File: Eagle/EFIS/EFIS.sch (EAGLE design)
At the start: 17 parts

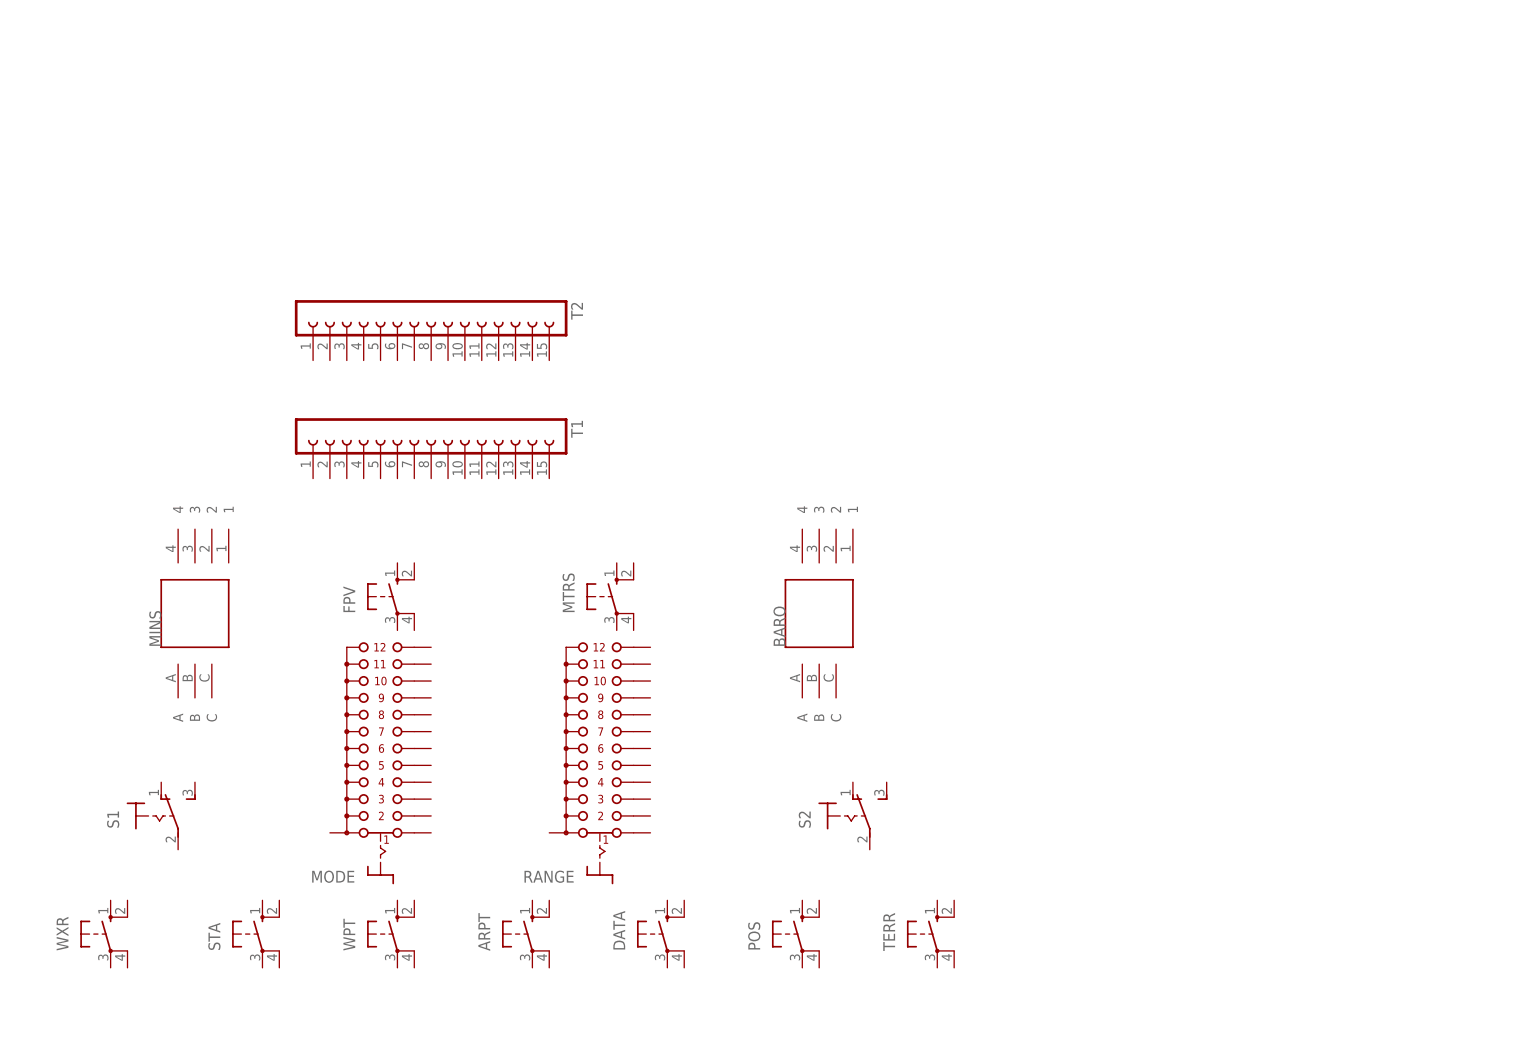
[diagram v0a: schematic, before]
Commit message: Button connections in Eagle
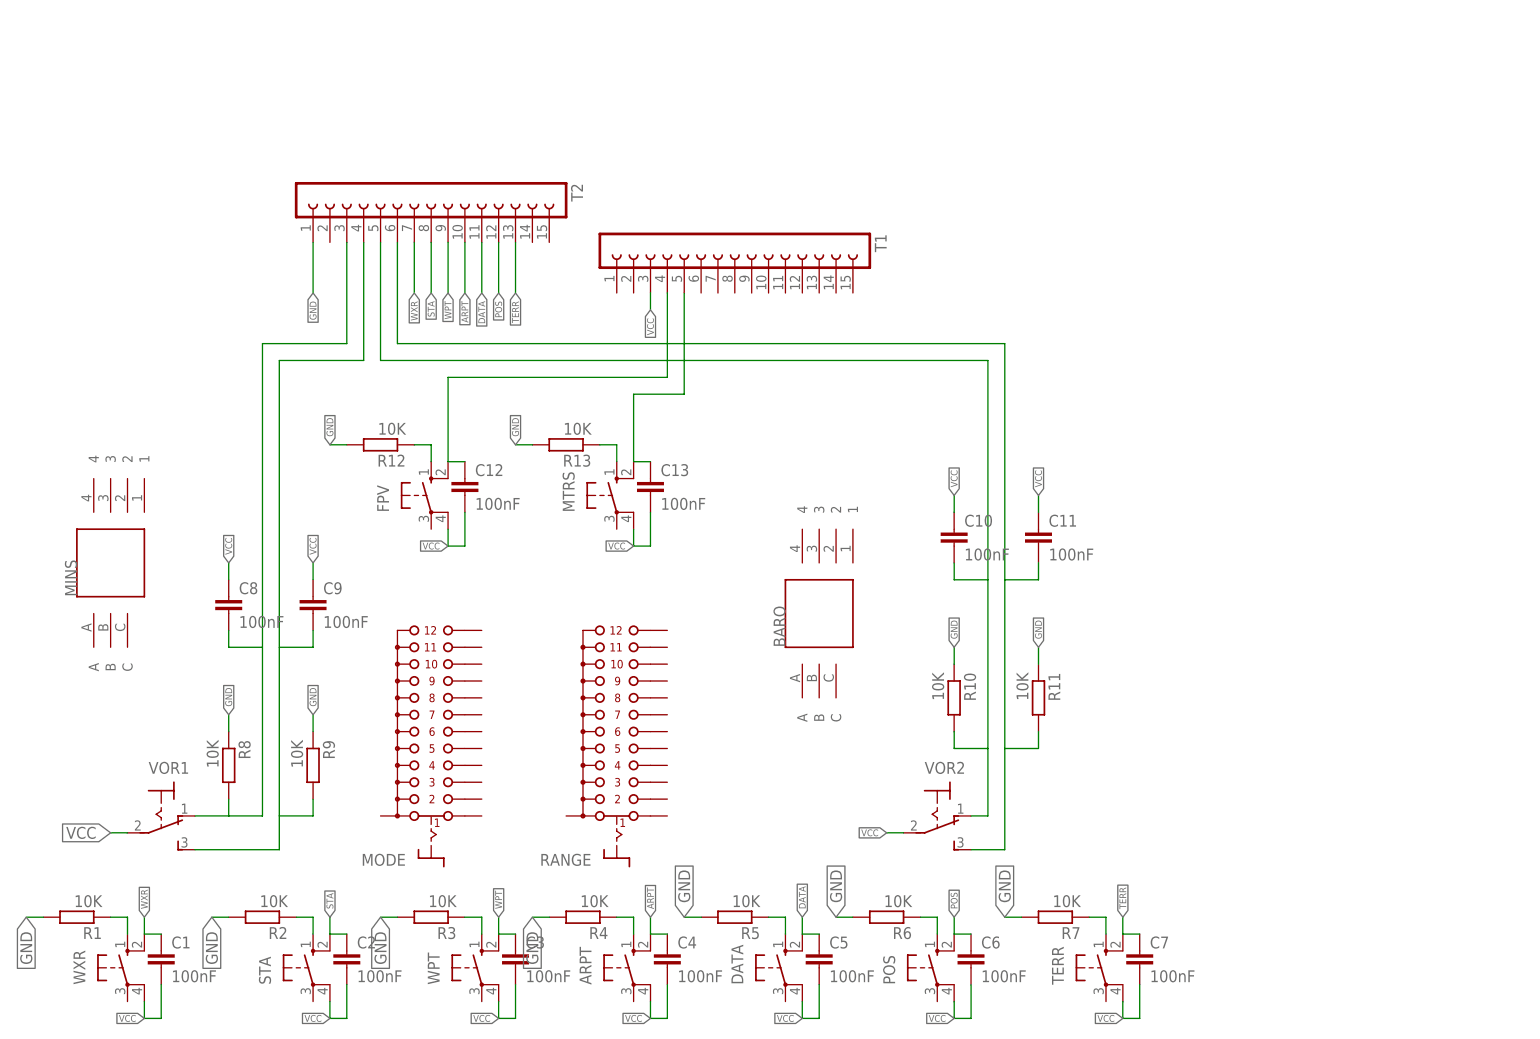
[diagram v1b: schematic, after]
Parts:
- removed S2: (no value), switch-custom:320-916
- added C1, C10, C11, C12, C13, C2, C3, C4, C5, C6, C7, C8, C9: 100nF, rcl:C-EUC1206
- added R1, R10, R11, R12, R13, R2, R3, R4, R5, R6, R7, R8, R9: 10K, resistor:R-EU_R1206
- added VOR2: (no value), switch-custom:320-916
- renumbered S1 to VOR1
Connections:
- new net ARPT: ARPT.S1, C4.1, T2.10
- new net DATA: C5.1, DATA.S1, T2.11
- new net GND: R1.2, R10.1, R11.1, R12.2, R13.2, R2.2, R3.2, R4.2, R5.2, R6.2, R7.2, R8.1, R9.1, T2.1
- new net N$1: R1.1, WXR.S
- new net N$10: POS.S, R6.1
- new net N$11: R7.1, TERR.S
- new net N$12: FPV.S, R12.1
- new net N$13: MTRS.S, R13.1
- new net N$14: C12.1, FPV.S1, T1.4
- new net N$15: C13.1, MTRS.S1, T1.5
- new net N$2: C8.2, R8.2, T2.3, VOR1.O
- new net N$3: C9.2, R9.2, T2.4, VOR1.S
- new net N$4: R2.1, STA.S
- new net N$5: R3.1, WPT.S
- new net N$6: C10.2, R10.2, T2.5, VOR2.O
- new net N$7: C11.2, R11.2, T2.6, VOR2.S
- new net N$8: ARPT.S, R4.1
- new net N$9: DATA.S, R5.1
- new net POS: C6.1, POS.S1, T2.12
- new net STA: C2.1, STA.S1, T2.8
- new net TERR: C7.1, T2.13, TERR.S1
- new net VCC: ARPT.P1, C1.2, C10.1, C11.1, C12.2, C13.2, C2.2, C3.2, C4.2, C5.2, C6.2, C7.2, C8.1, C9.1, DATA.P1, FPV.P1, MTRS.P1, POS.P1, STA.P1, T1.3, TERR.P1, VOR1.P, VOR2.P, WPT.P1, WXR.P1
- new net WPT: C3.1, T2.9, WPT.S1
- new net WXR: C1.1, T2.7, WXR.S1
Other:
- moved on the sheet: ARPT, DATA, FPV, MINS, MODE, MTRS, POS, RANGE, STA, T1, T2, TERR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

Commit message: All components placed and some manual routing
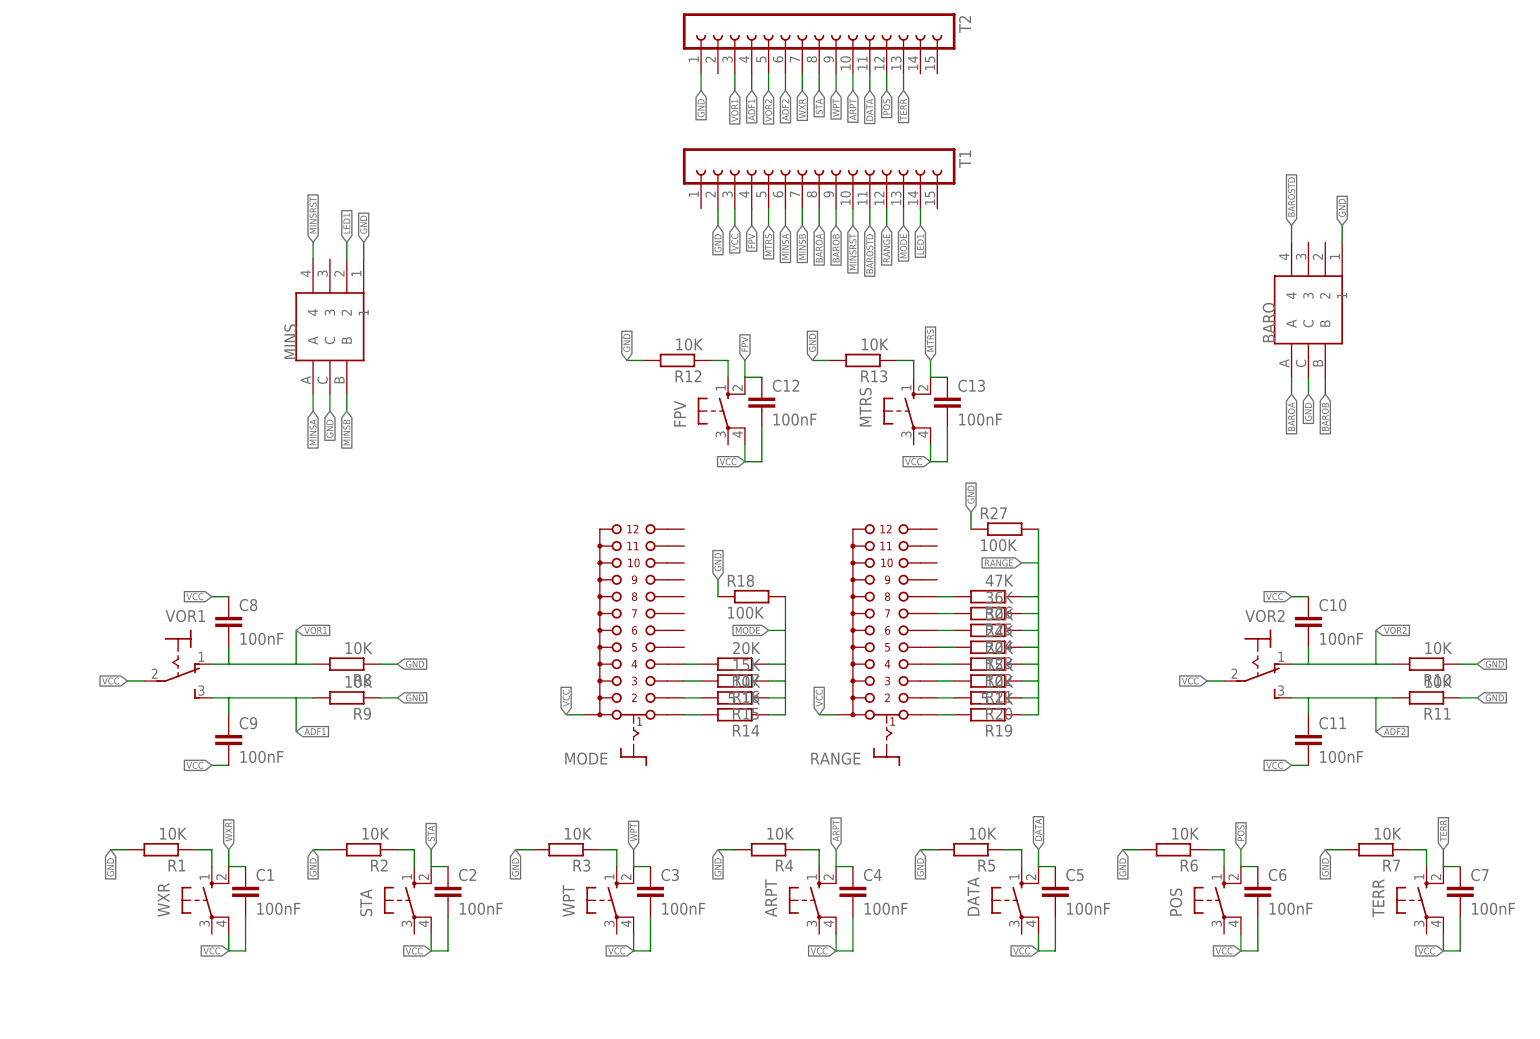
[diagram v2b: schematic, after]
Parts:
- added R14, R19: 5.1K, resistor:R-EU_R1206
- added R15, R20: 10K, resistor:R-EU_R1206
- added R16, R21: 15K, resistor:R-EU_R1206
- added R17, R22: 20K, resistor:R-EU_R1206
- added R18, R27: 100K, resistor:R-EU_R1206
- added R23: 24K, resistor:R-EU_R1206
- added R24: 30K, resistor:R-EU_R1206
- added R25: 36K, resistor:R-EU_R1206
- added R26: 47K, resistor:R-EU_R1206
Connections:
- net N$14 renamed FPV
- net N$15 renamed MTRS
- net N$2 renamed VOR1
- net N$6 renamed VOR2
- removed net N$3: C9.2, R9.2, T2.4, VOR1.S
- removed net N$7: C11.2, R11.2, T2.6, VOR2.S
- new net ADF1: C9.1, R9.2, T2.4, VOR1.S
- new net ADF2: C11.1, R11.2, T2.6, VOR2.S
- new net BAROA: BARO.A, T1.8
- new net BAROB: BARO.B, T1.9
- new net BAROSTD: BARO.4, T1.11
- new net LED1: MINS.2, T1.14
- new net MINSA: MINS.A, T1.6
- new net MINSB: MINS.B, T1.7
- new net MINSRST: MINS.4, T1.10
- new net MODE: R14.1, R15.1, R16.1, R17.1, R18.2, T1.13
- new net N$16: MODE.1, R14.2
- new net N$17: MODE.2, R15.2
- new net N$18: MODE.3, R16.2
- new net N$19: MODE.4, R17.2
- new net N$21: R19.2, RANGE.1
- new net N$22: R20.2, RANGE.2
- new net N$23: R21.2, RANGE.3
- new net N$24: R22.2, RANGE.4
- new net N$25: R23.2, RANGE.5
- new net N$26: R24.2, RANGE.6
- new net N$27: R25.2, RANGE.7
- new net N$28: R26.2, RANGE.8
- new net RANGE: R19.1, R20.1, R21.1, R22.1, R23.1, R24.1, R25.1, R26.1, R27.2, T1.12
- net GND: now also BARO.1, BARO.C, MINS.1, MINS.C, R18.1, R27.1, T1.2
- net VCC: now also C11.2, C9.2, MODE.A, RANGE.A; no longer C11.1, C9.1
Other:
- moved on the sheet: ARPT, BARO, C1, C10, C11, C12, C13, C2, C3, C4, C5, C6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

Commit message: REV 1 PCB
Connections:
- net MODE: now also T1.12; no longer T1.13
- net RANGE: now also T1.13; no longer T1.12
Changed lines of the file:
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@@
 <net name="MODE" class="0">
-<segment>
-<pinref part="T1" gate="G$1" pin="13"/>
-<wire x1="129.54" y1="116.84" x2="129.54" y2="114.3" width="0.1524" layer="91"/>
-<label x="129.54" y="114.3" size="1.016" layer="95" rot="R270" xref="yes"/>
-</segment>
 <segment>
 <pinref part="R16" gate="G$1" pin="1"/>
@@
 <label x="109.22" y="53.34" size="1.016" layer="95" rot="R180" xref="yes"/>
 </segment>
-</net>
-<net name="RANGE" class="0">
 <segment>
 <pinref part="T1" gate="G$1" pin="12"/>
@@
 <label x="127" y="114.3" size="1.016" layer="95" rot="R270" xref="yes"/>
 </segment>
+</net>
+<net name="RANGE" class="0">
 <segment>
 <pinref part="R26" gate="G$1" pin="1"/>
@@
 <label x="147.32" y="63.5" size="1.016" layer="95" rot="R180" xref="yes"/>
 </segment>
+<segment>
+<pinref part="T1" gate="G$1" pin="13"/>
+<wire x1="129.54" y1="116.84" x2="129.54" y2="114.3" width="0.1524" layer="91"/>
+<label x="129.54" y="114.3" size="1.016" layer="95" rot="R270" xref="yes"/>
+</segment>
 </net>
